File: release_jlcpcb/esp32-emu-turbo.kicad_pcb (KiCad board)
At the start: 4 copper layers, 160 x 75 mm, 82 parts, among them J1 USB-C-16P, J3 JST-PH-2P, J4 FPC-40P-0.5mm, SW1 SW-SMD-5.1x5.1, SW10 SW-SMD-5.1x5.1, SW11 SW-SMD-5.1x5.1, SW12 SW-SMD-5.1x5.1, SW13 SW-SMD-5.1x5.1, SW2 SW-SMD-5.1x5.1, SW3 SW-SMD-5.1x5.1, SW4 SW-SMD-5.1x5.1, SW5 SW-SMD-5.1x5.1, SW6 SW-SMD-5.1x5.1, SW7 SW-SMD-5.1x5.1, SW8 SW-SMD-5.1x5.1, SW9 SW-SMD-5.1x5.1, U1 ESP32-S3-WROOM-1-N16R8, U2 ESOP-8, U3 SOT-223, U5 SOP-16, U6 TF-01A

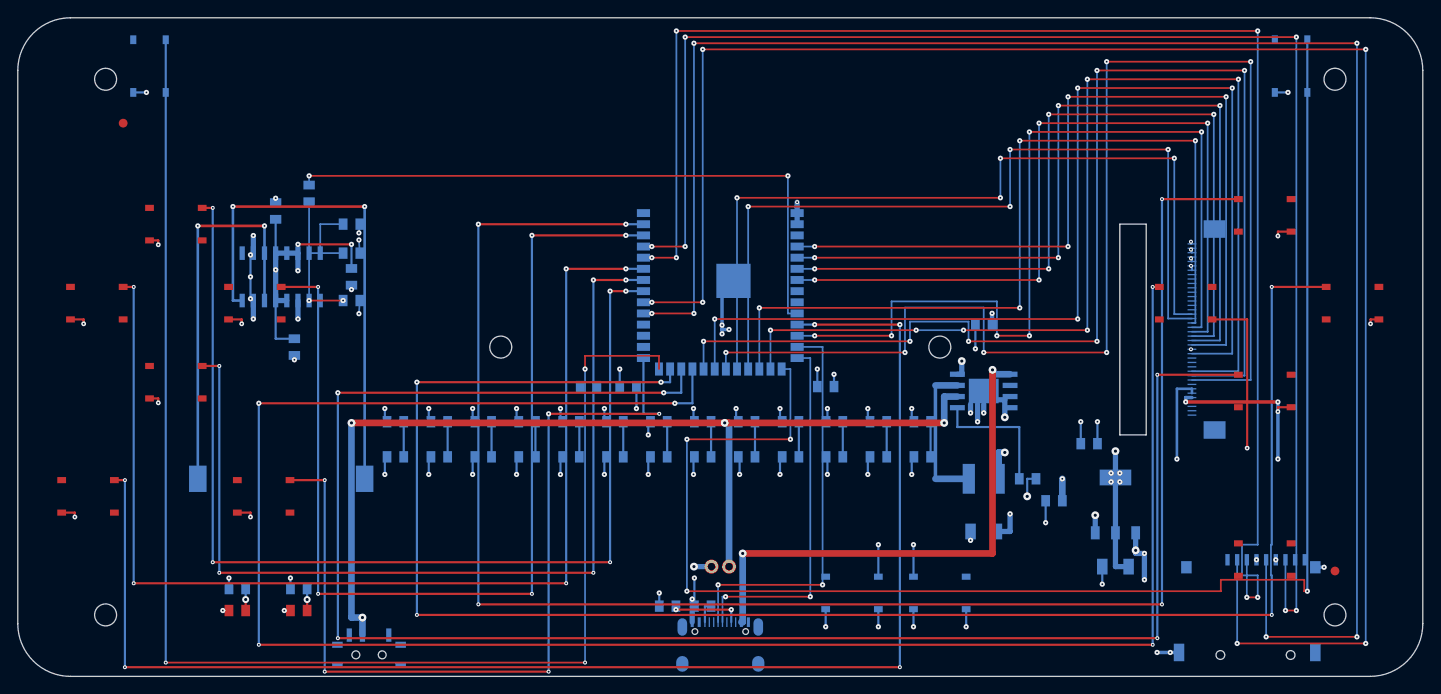
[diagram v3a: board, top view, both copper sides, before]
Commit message: fix(pcb): USB meander + ESP32 bypass cap + VIA_MIN increase for 95% confidence
3 fixes to bring manufacturing confidence from 89% to 95%:

1. USB D+/D- length matching: 3-loop meander on D+ F.Cu (amplitude=0.50mm)
   Mismatch reduced from 4.57mm to 1.57mm (target <2mm) ✓

2. ESP32 VDD bypass cap: C26 (100nF 0805) at (91.5, 21.0) on B.Cu
   3.6mm from U1 pin 2 (+3V3), was 17.9mm (nearest C3) ✓

3. Via annular ring: VIA_MIN 0.46→0.50mm (AR 0.13→0.15mm)
   Matches JLCPCB recommended minimum, eliminates 77 warnings ✓

4. Fiducials already present (FID1/FID2 at diagonal corners) ✓

Verified: DFM 114/114, DFA 9/9, Polarity 40/40.
release_jlcpcb/ synced (gerbers, BOM, CPL, kicad_pcb).

Co-Authored-By: Claude Opus 4.6 (1M context) <noreply@anthropic.com>
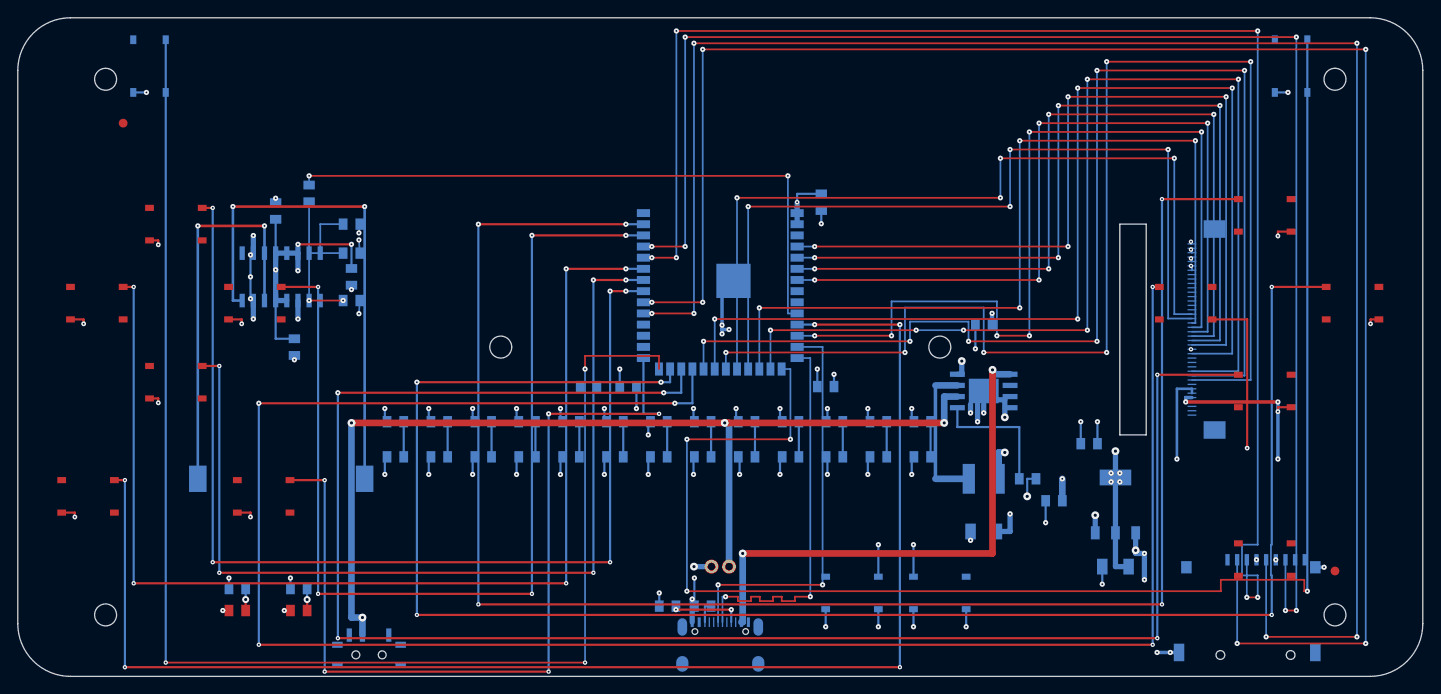
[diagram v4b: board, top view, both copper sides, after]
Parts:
- removed the C22 at (33.2, 20.0)
- removed the SW7 at (142.0, 42.5)
- removed the SW_RST at (95.0, 65.5)
- removed the U6 at (140.0, 67.0)
- added C26: C_0805, C_0805, B.Cu at (91.5, 21.0)
- added FID1: Fiducial, Fiducial, F.Cu at (12.0, 12.0)
- added LED1: LED_0805, LED_0805, F.Cu at (25.0, 67.5)
- added R17: R_0805, R_0805, B.Cu at (25.0, 65.0)
- added U2: ESOP-8, ESOP-8, B.Cu at (110.0, 42.5)
- C22: renamed from FID1; value Fiducial -> C_0805; footprint Fiducial -> C_0805; moved to B.Cu
- SW7: renamed from LED1; value LED_0805 -> SW-SMD-5.1x5.1; footprint LED_0805 -> SW-SMD-5.1x5.1
- SW_RST: renamed from R17; value R_0805 -> SW-SMD-5.1x5.1; footprint R_0805 -> SW-SMD-5.1x5.1
- U6: renamed from U2; value ESOP-8 -> TF-01A; footprint ESOP-8 -> TF-01A
- moved SW7 119.6 mm to (142.0, 42.5)
- moved SW_RST 70.0 mm to (95.0, 65.5)
- moved U6 38.7 mm to (140.0, 67.0)
- moved C22 22.6 mm to (33.2, 20.0)
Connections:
- C22 pad 1: (no net) -> I2S_DOUT
- SW7 pad 1: GND -> BTN_X
- SW7 pad 2: LED1_RA -> (no net)
- SW_RST pad 1: LED1_RA -> EN
- SW_RST pad 2: +3V3 -> (no net)
- U6 pad 1: VBUS -> (no net)
- U6 pad 2: (no net) -> SD_CS
- U6 pad 3: (no net) -> SD_MOSI
- U6 pad 4: (no net) -> +3V3
- U6 pad 5: IP5306_KEY -> SD_CLK
- U6 pad 6: BAT+ -> GND
- U6 pad 7: LX -> SD_MISO
- U6 pad 8: +5V -> (no net)
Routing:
- net +3V3: track 58.9 -> 62.6 mm
- net USB_D+: track 41.6 -> 44.6 mm
- net GND: track 164.6 -> 166.1 mm, vias 75 -> 76
